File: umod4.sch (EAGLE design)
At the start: 86 parts, among them IC3 27C256-FEED-THRU, J1 DMSAT-SF-PEJ, J2 10118194-0001LF, J4 CORTEX_DEBUG-PTH, J5 C160394/JST BM08B-SRSS, J6 CORTEX_DEBUG-PTH, M1 RPi Pico W, M2 Generic single-sided NEO-8, Q1 C10487/SI2301CDS, Q2 C2150/SS8050, U1 C113281/74LVC541, U2 C6091/74LVC4245, U3 C113281/74LVC541, U4 C2040/RP2040, U5 C97521/W25Q128JVSIQ, U6 C10428/74LVC2G04, U7 C10428/74LVC2G04, U8 WS2812C-2020, U9 TPS560430X, Y1 C9002/12MHz

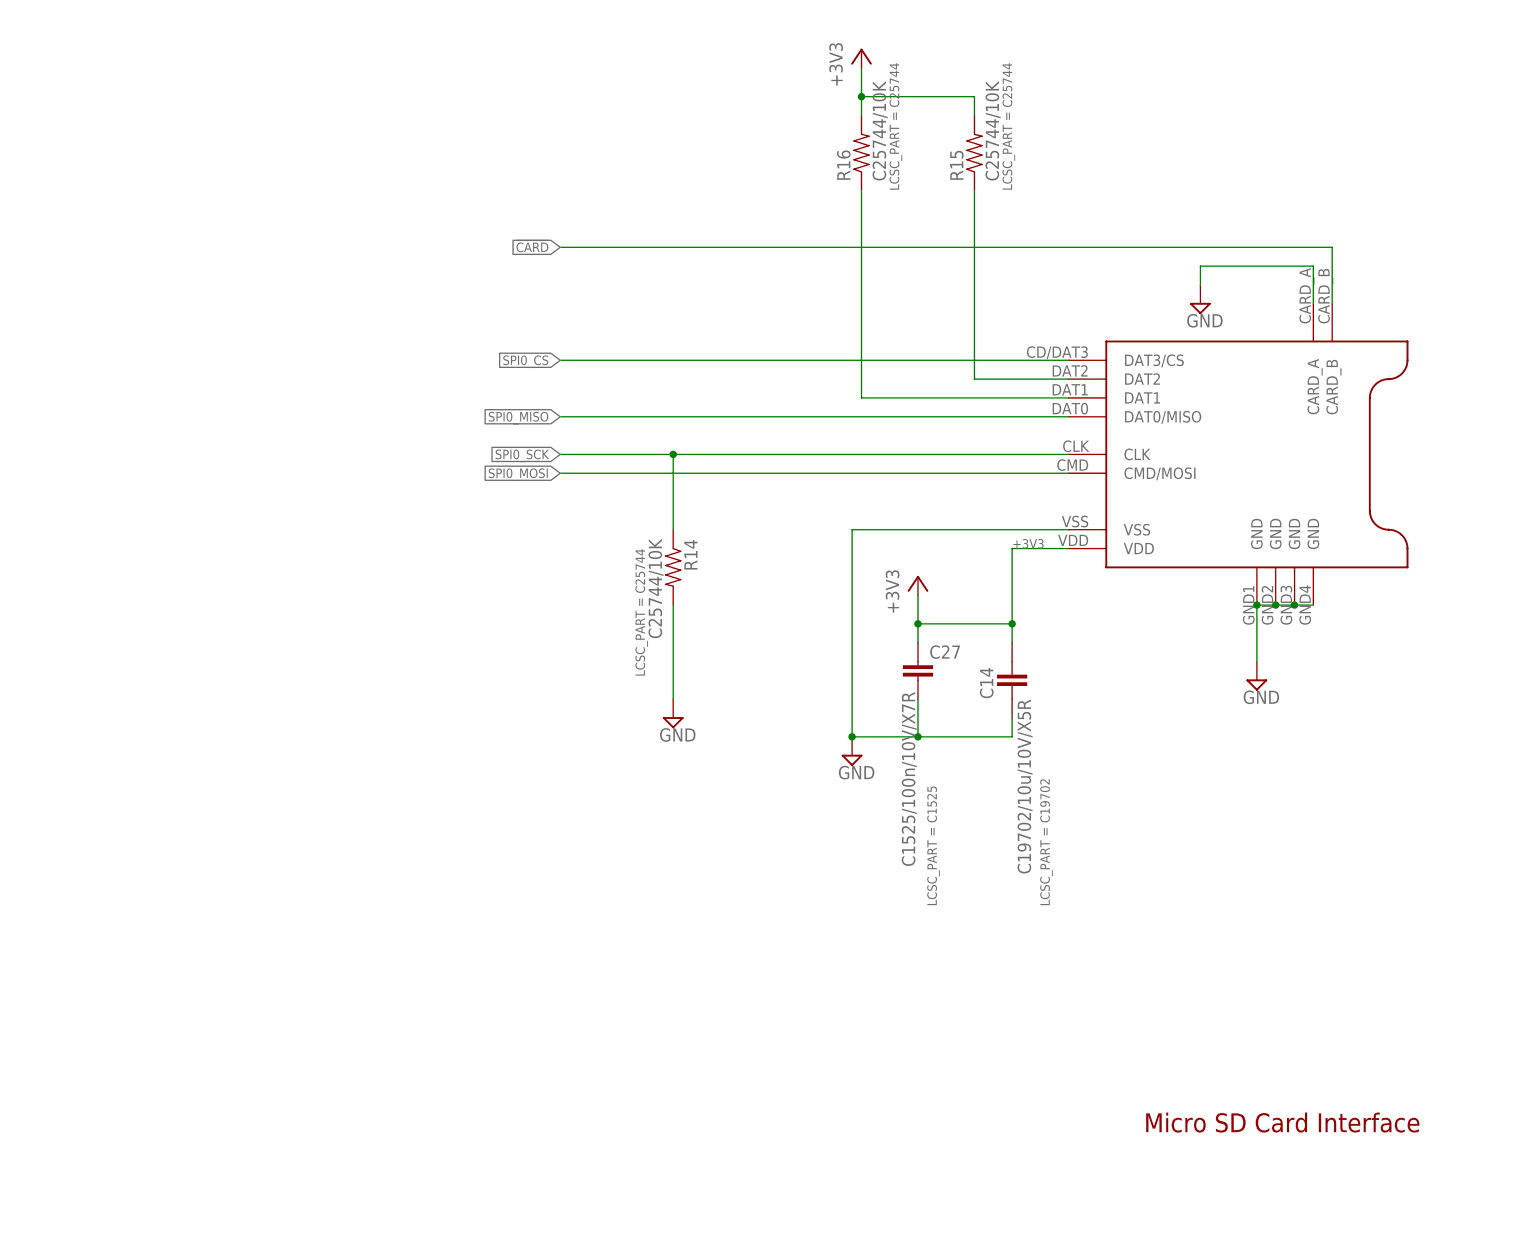
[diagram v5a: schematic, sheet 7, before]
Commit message: Power supply design updates
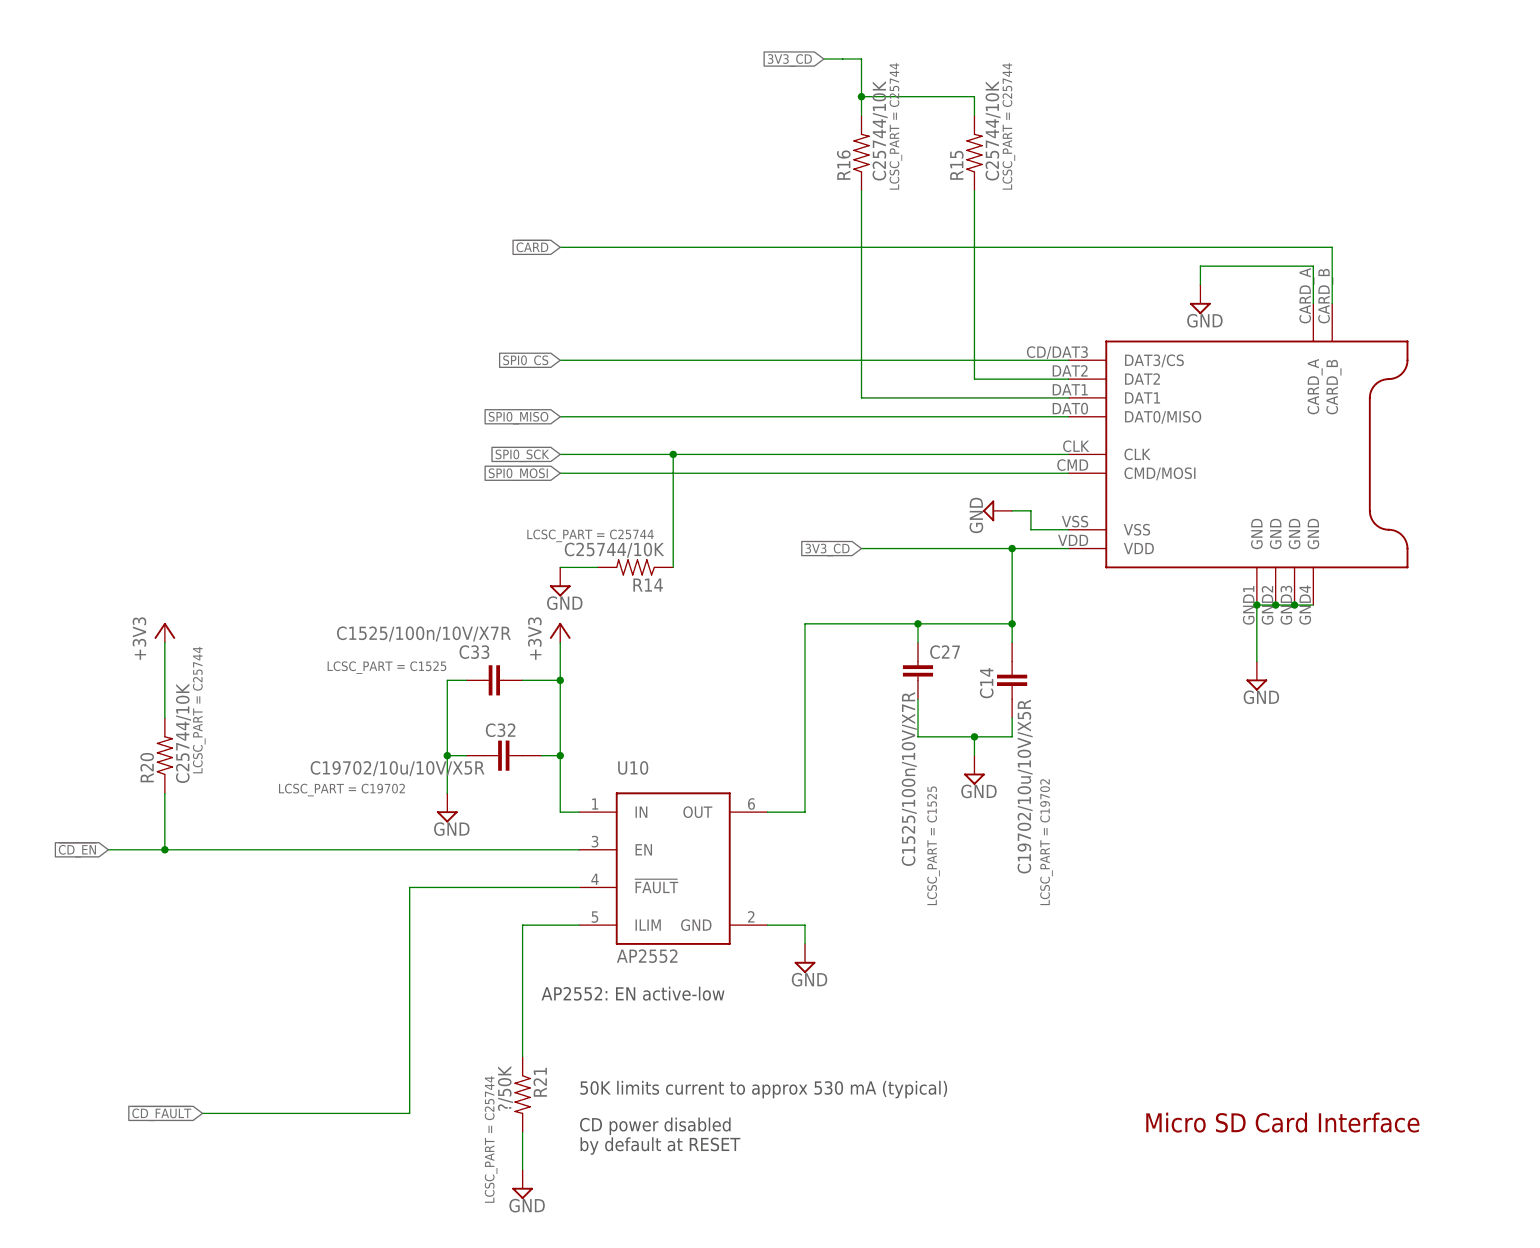
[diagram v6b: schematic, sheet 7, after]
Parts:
- removed J6: CORTEX_DEBUG-PTH, robins-v7:CORTEX_DEBUG-PTH
- removed S2: (no value), robins-v7:SWITCH-TAC-5.2MM
- added C32: C19702/10u/10V/X5R, ipc-7351-capacitor:CAPACITOR_0603
- added C33: C1525/100n/10V/X7R, SparkFun-03-01-2010:CAP0402-CAP
- added F1: FUSEPICOFUSE, fuse:FUSEPICOFUSE
- added R20: C25744/10K, SparkFun-03-01-2010:RESISTOR0402-RES
- added R21: ?/50K, SparkFun-03-01-2010:RESISTOR0402-RES
- added U10: AP2552, robins-v7:AP2552/3SOT23-6
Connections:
- net +5V renamed +5_ECU
- removed net WP_SDIO: J6.SWDIO, M1.SWDIO
- removed net WP_SWCLK: J6.SWDCLK, M1.SWCLK
- new net !CD_EN: R20.1, U10.EN
- new net !CD_FAULT: U10.!FAULT
- new net 3V3_CD: C14.2, C27.1, J1.VDD, R15.2, R16.2, U10.OUT
- new net N$19: C13.1, C28.1, F1.2, U9.VIN
- new net N$25: R21.1, U10.ILIM
- net +12_US: now also F1.1; no longer C13.1, C28.1, U9.VIN
- net +3V3: now also C32.2, C33.2, R20.2, U10.IN; no longer C14.2, C27.1, J1.VDD, J6.VCC, R15.2, R16.2
- net GND: now also C32.1, C33.1, R21.2, U10.GND; no longer J6.GND, S2.2
- net SPARE0: no longer S2.1
- net WP_RUN: no longer J6.!RESET
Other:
- note added: "50K limits current to approx 530 mA (typical)"
- note added: "AP2552: EN active-low"
- note added: "CD power disabled by default at RESET"
- moved on the sheet: R14

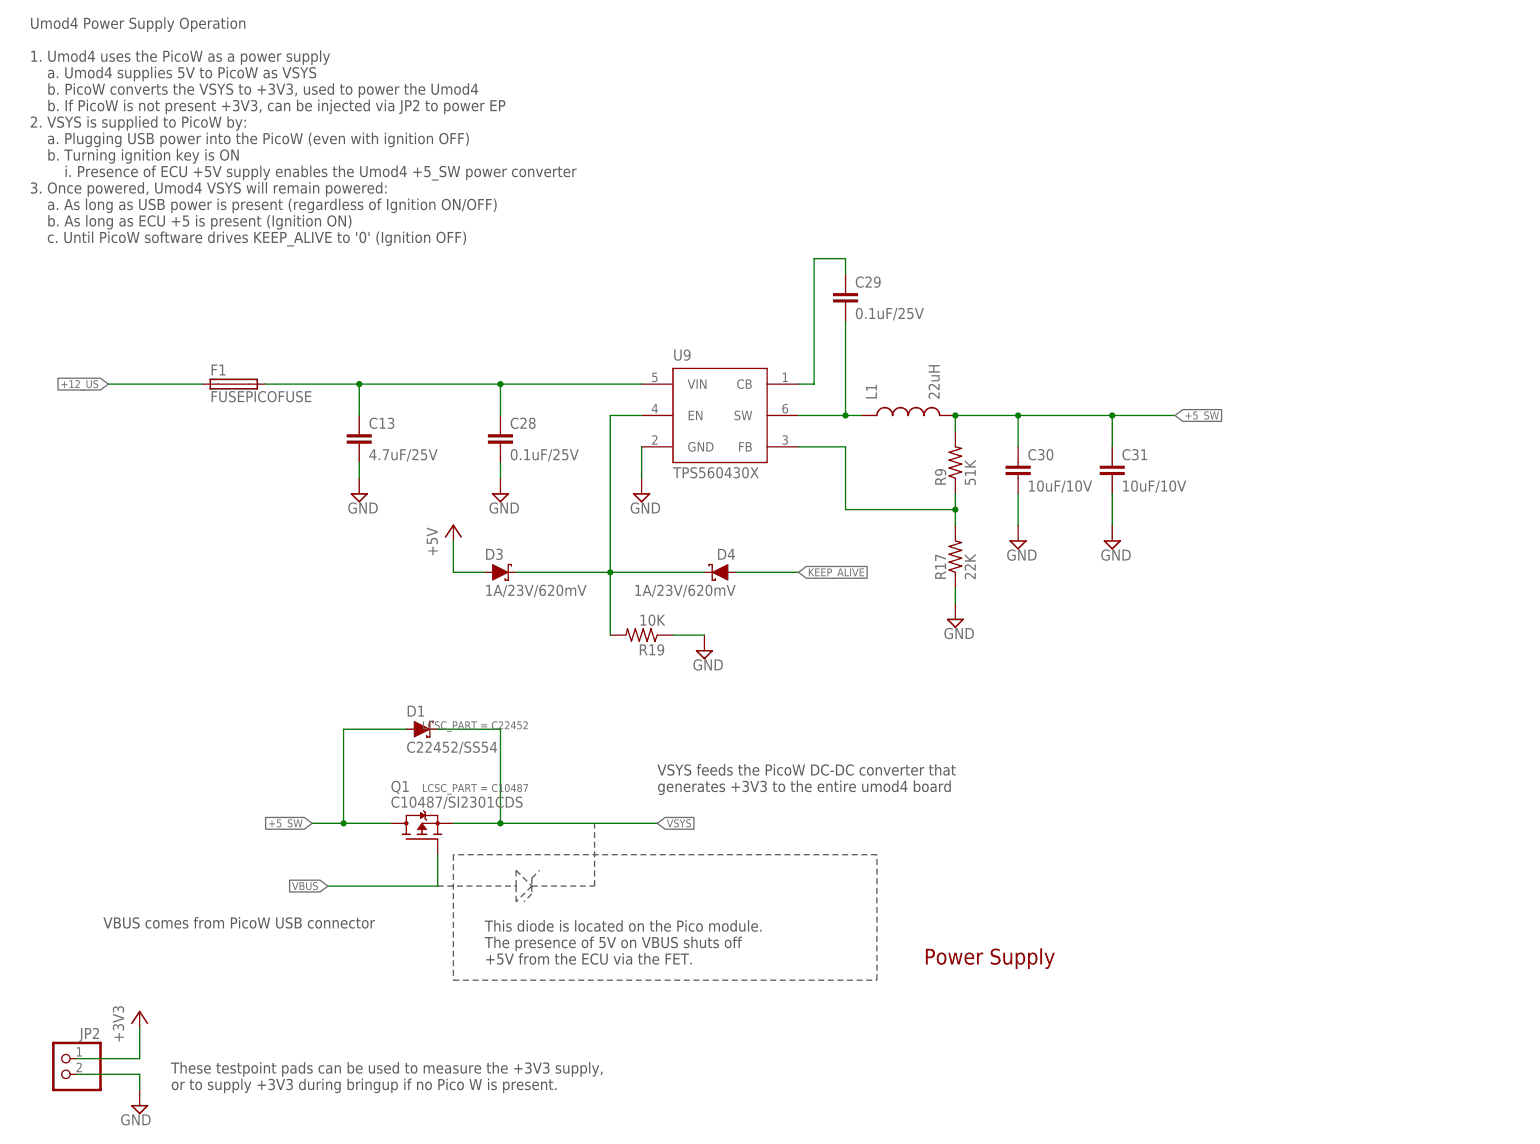
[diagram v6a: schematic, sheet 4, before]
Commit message: Removed SD power switch
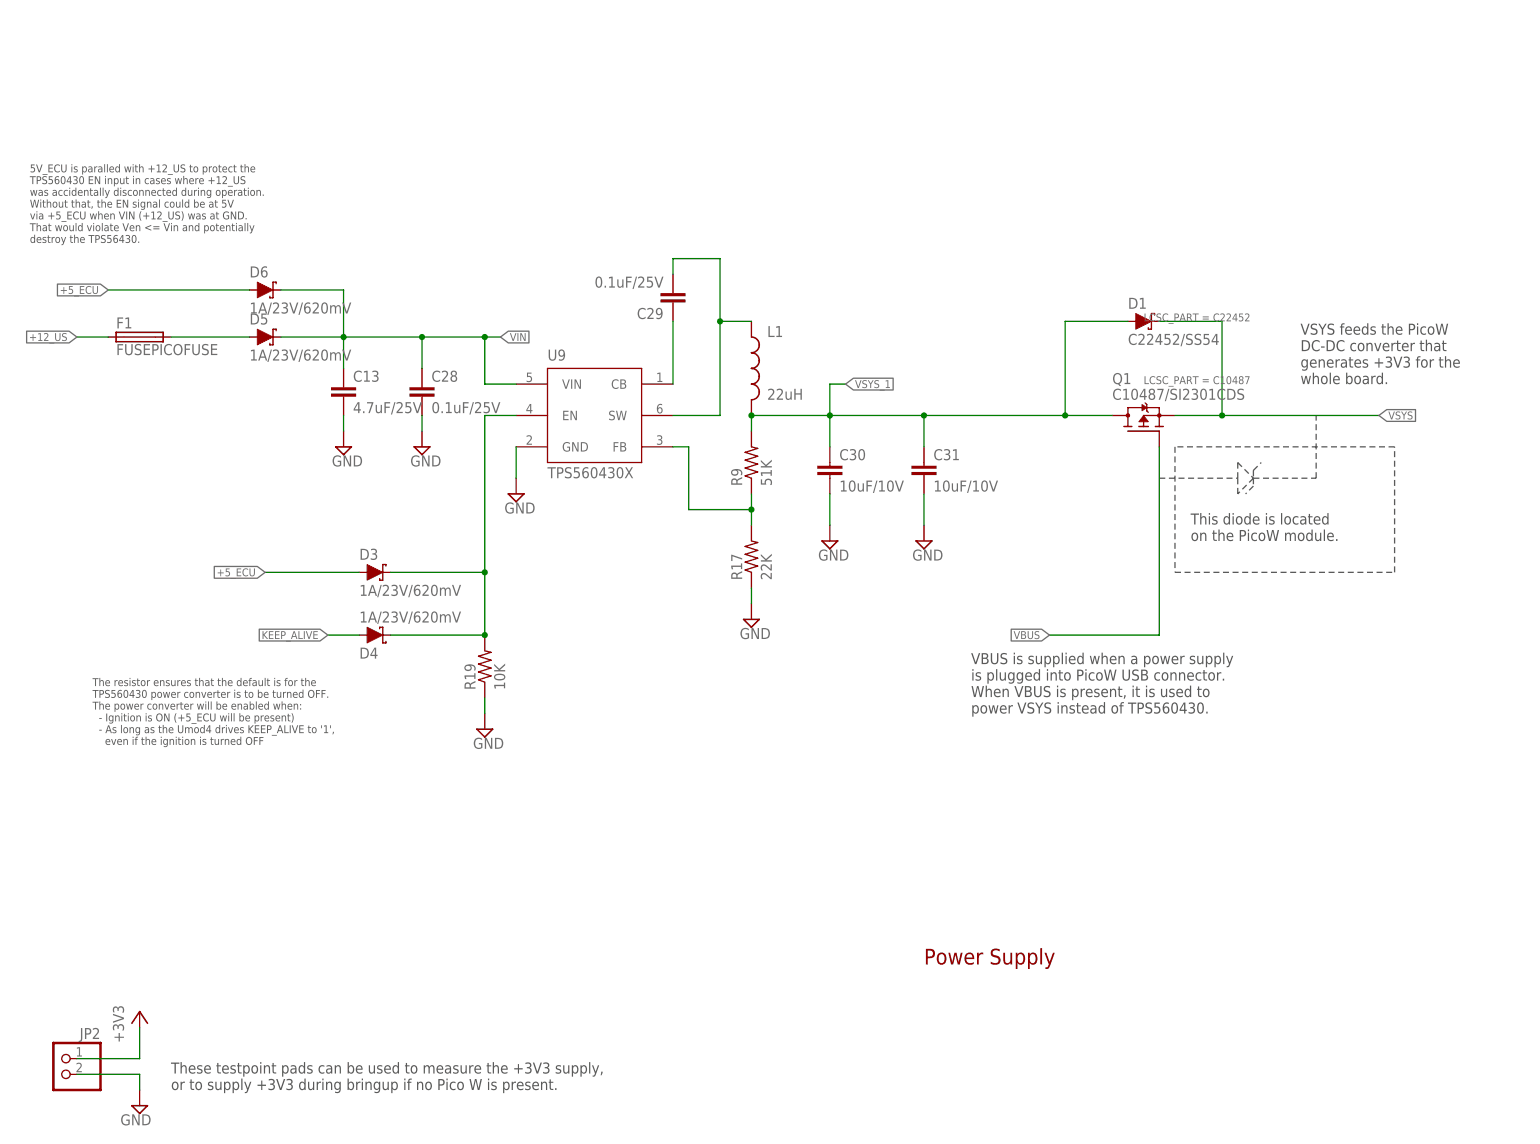
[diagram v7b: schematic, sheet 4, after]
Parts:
- added D5, D6: 1A/23V/620mV, SparkFun-DiscreteSemi:DIODE-SCHOTTKY-BAT20J
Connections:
- net +5_SW renamed VSYS_1
- removed net N$19: C13.1, C28.1, F1.2, U9.VIN
- new net N$24: D5.A, F1.2
- new net VIN: C13.1, C28.1, D5.C, D6.C, U9.VIN
- net +5_ECU: now also D6.A
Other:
- note added: "5V_ECU is paralled with +12_US to protect the TPS560430 EN input in cases where +12_US was accidentally disconnected during operation. Without that, the EN signal could be at 5V via +5_ECU when VIN (+12_US) was at GND. That would violate Ven <= Vin and potentially destroy the TPS56430."
- note added: "The resistor ensures that the default is for the TPS560430 power converter is to be turned OFF. The power converter will be enabled when: - Ignition is ON (+5_ECU will be present) - As long as the Umod4 drives KEEP_ALIVE to '1', even if the ignition is turned OFF"
- note added: "This diode is located on the PicoW module."
- note added: "VBUS is supplied when a power supply is plugged into PicoW USB connector. When VBUS is present, it is used to power VSYS instead of TPS560430."
- note added: "VSYS feeds the PicoW DC-DC converter that generates +3V3 for the whole board."
- note removed: "This diode is located on the Pico module. The presence of 5V on VBUS shuts off +5V from the ECU via the FET."
- note removed: "Umod4 Power Supply Operation 1. Umod4 uses the PicoW as a power supply a. Umod4 supplies 5V to PicoW as VSYS b. PicoW converts the VSYS to +3V3, used to power the Umod4 b. If PicoW is not present +3V3, can be injected via JP2 to power EP 2. VSYS is supplied to PicoW by: a. Plugging USB power into the PicoW (even with ignition OFF) b. Turning ignition key is ON i. Presence of ECU +5V supply enable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"
- note removed: "VBUS comes from PicoW USB connector"
- note removed: "VSYS feeds the PicoW DC-DC converter that generates +3V3 to the entire umod4 board"
- moved on the sheet: C13, C28, C29, C30, C31, D1, D3, D4, F1, L1, Q1, R17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

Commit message: Before rotating SPI connector
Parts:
- removed C32: C19702/10u/10V/X5R, ipc-7351-capacitor:CAPACITOR_0603
- removed C33: C1525/100n/10V/X7R, SparkFun-03-01-2010:CAP0402-CAP
- removed R21: ?/50K, SparkFun-03-01-2010:RESISTOR0402-RES
- removed U10: AP2552, robins-v7:AP2552/3SOT23-6
- added J3: (no value), robins-v7:FASTON-TABHORIZONTAL-MALE
- C14: value C19702/10u/10V/X5R -> C1525/100n/10V/X7R; device ipc-7351-capacitor:CAPACITOR_0603 -> SparkFun-03-01-2010:CAP0402-CAP; LCSC_PART C19702 -> C1525
- C27: value C1525/100n/10V/X7R -> C368809/4u7/10V/X5R; LCSC_PART C1525 -> C368809
- R20: value C25744/10K -> S10K40; device SparkFun-03-01-2010:RESISTOR0402-RES -> varistor:S10K40; LCSC_PART C25744 -> (none)
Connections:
- removed net !CD_EN: R20.1, U10.EN
- removed net !CD_FAULT: U10.!FAULT
- removed net 3V3_CD: C14.2, C27.1, J1.VDD, R15.2, R16.2, U10.OUT
- removed net N$25 (its old number): R21.1, U10.ILIM
- net +12_US: now also J3.1, R20.2
- net +3V3: now also C14.1, C27.1, J1.VDD, R15.2, R16.2; no longer C32.2, C33.2, R20.2, U10.IN
- net GND: now also C14.2, R20.1; no longer C14.1, C32.1, C33.1, R21.2, U10.GND
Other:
- note added: "These parts are located on the PicoW module."
- note added: "When USB cable is unplugged, VBUS may drop slow enough that Q1 does not turn on very quickly. D1 provides power until Q1 is ON."
- note removed: "50K limits current to approx 530 mA (typical)"
- note removed: "AP2552: EN active-low"
- note removed: "CD power disabled by default at RESET"
- note removed: "This diode is located on the PicoW module."
- moved on the sheet: C13, C14, C27, C28, C29, C30, C31, D1, D3, D4, D5, D6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
